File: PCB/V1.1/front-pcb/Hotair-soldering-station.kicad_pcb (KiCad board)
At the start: 2 copper layers, 99.4 x 61 mm, 24 parts, among them J1 Conn_01x03, J2 main-board-conn, J3 hot_on, SW1 HOTAIR_UP, SW2 HOTAIR_DOWN, SW3 SIRON_UP, SW4 SIRON_DOWN, SW5 FAN_UP, SW6 FAN_DOWN, SW7 MENU_UP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

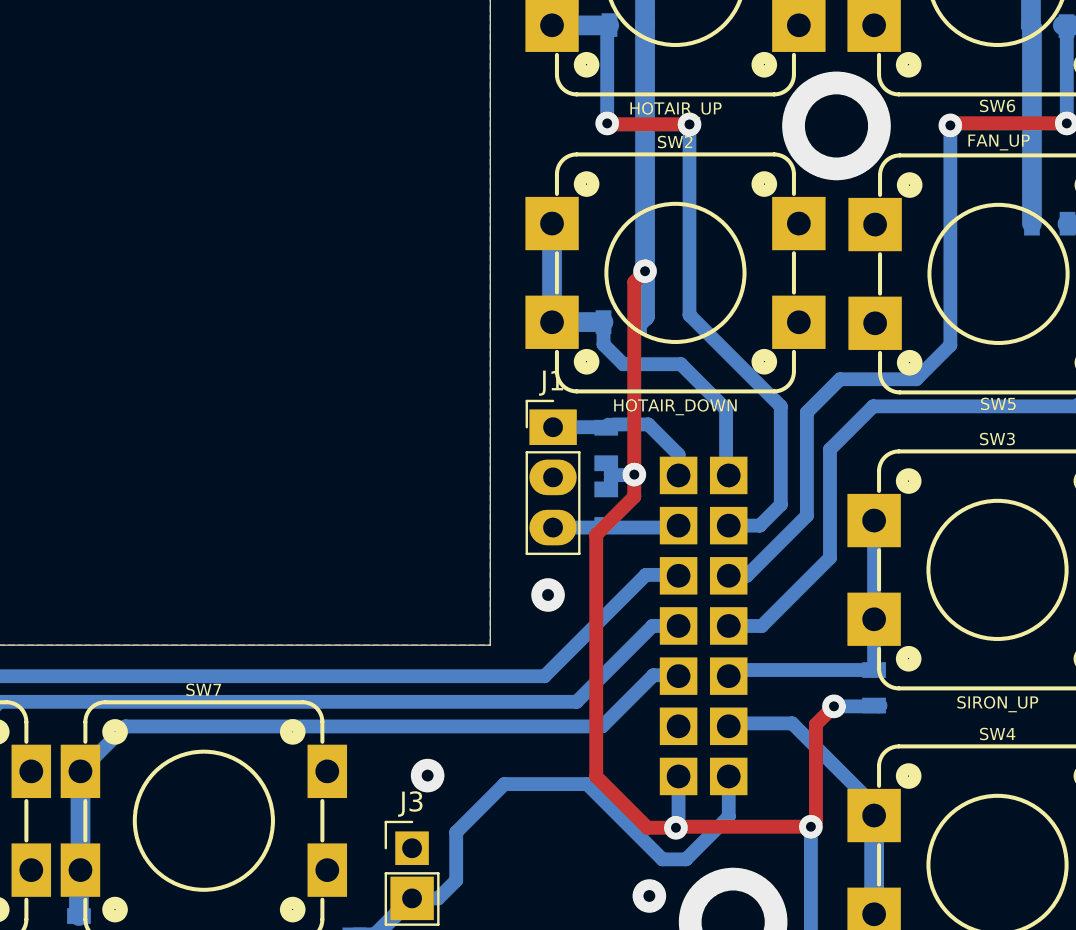
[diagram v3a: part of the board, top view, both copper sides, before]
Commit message: Larger IDC conenctor pads for front panel
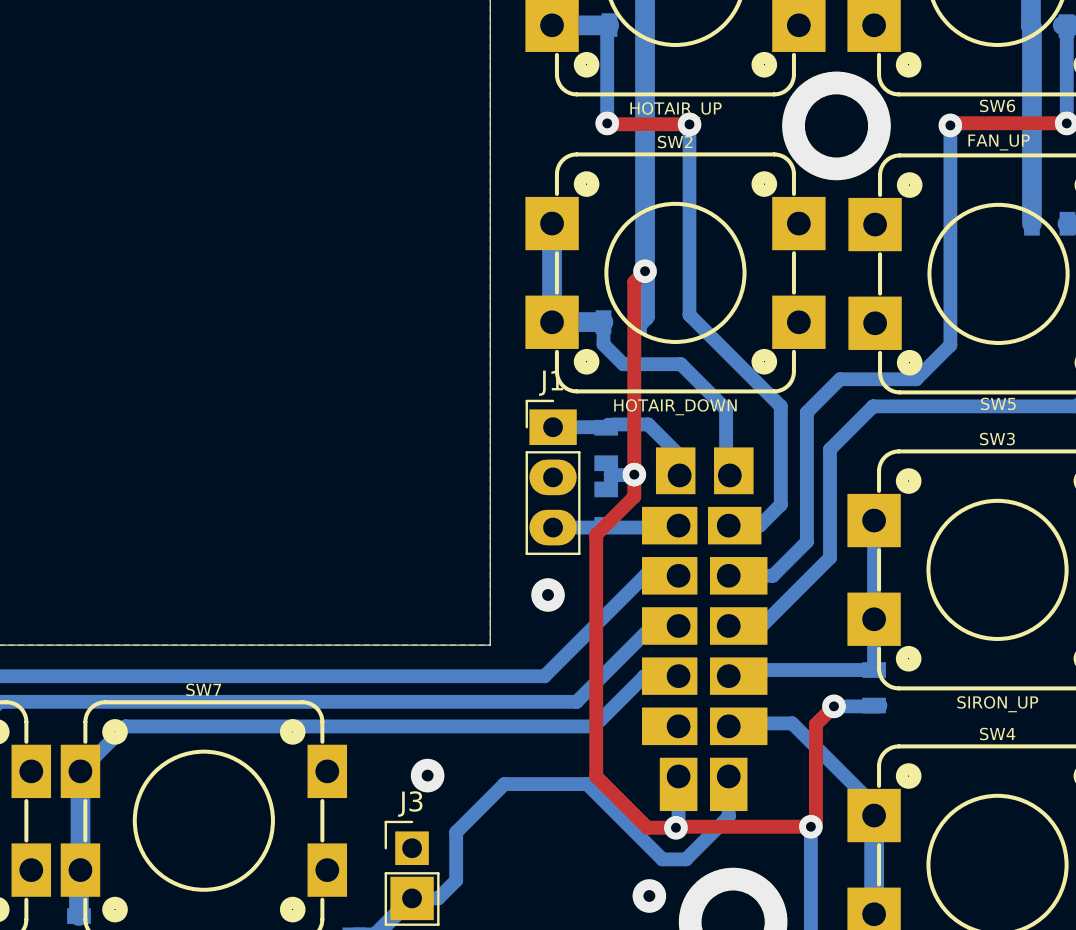
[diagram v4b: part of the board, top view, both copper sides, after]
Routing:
- net MENU_UP_SW: track 39.5 -> 40.8 mm
- net HOTAIR_FAN_DOWN_SW: track 49.1 -> 49.9 mm
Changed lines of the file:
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@@
     (property "Sheetname" "")
     (attr through_hole)
-    (fp_text reference "J2" (at 0 -0.5) (layer "B.SilkS")
+    (fp_text reference "J2" (at 0 -0.5 180) (layer "B.SilkS")
       (effects (font (size 1 1) (thickness 0.15)) (justify mirror))
     )
-    (fp_text value "main-board-conn" (at 0 0.5) (layer "B.Fab")
+    (fp_text value "main-board-conn" (at 0 0.5 180) (layer "B.Fab")
       (effects (font (size 1 1) (thickness 0.15)) (justify mirror))
     )
-    (fp_text user "REF**" (at 3.12 0.58) (layer "B.SilkS")
+    (fp_text user "REF**" (at 3.12 0.58 180) (layer "B.SilkS")
       (effects (font (size 1 1) (thickness 0.15)) (justify mirror))
     )
-    (fp_text user "${REFERENCE}" (at 3.12 -9.37 90) (layer "B.Fab")
+    (fp_text user "${REFERENCE}" (at 3.12 -9.37 -90) (layer "B.Fab")
       (effects (font (size 1 1) (thickness 0.15)) (justify mirror))
     )
@@
     (fp_line (start 5.66 -0.48) (end 5.66 -18.26) (layer "B.Fab") (width 0.1))
     (fp_line (start 0.58 -18.26) (end 0.58 -1.75) (layer "B.Fab") (width 0.1))
-    (pad "1" thru_hole rect locked (at 1.85 -1.75) (size 1.9 1.9) (drill 1.2) (layers *.Cu *.Mask)
+    (pad "1" thru_hole rect (at 1.85 -1.75) (size 1.9 2.7) (drill 1.2 (offset 0 0.4)) (layers *.Cu *.Mask)
       (net 7 "+3V3") (pinfunction "Pin_1") (pintype "passive"))
-    (pad "2" thru_hole rect locked (at 1.85 -4.29) (size 1.9 1.9) (drill 1.2) (layers *.Cu *.Mask)
+    (pad "2" thru_hole rect (at 1.85 -4.29) (size 2.8 1.9) (drill 1.2 (offset -0.45 0)) (layers *.Cu *.Mask)
       (net 6 "GND") (pinfunction "Pin_2") (pintype "passive"))
-    (pad "3" thru_hole rect locked (at 1.85 -6.83) (size 1.9 1.9) (drill 1.2) (layers *.Cu *.Mask)
+    (pad "3" thru_hole rect (at 1.85 -6.83) (size 2.8 1.9) (drill 1.2 (offset -0.45 0)) (layers *.Cu *.Mask)
       (net 8 "MENU_UP_SW") (pinfunction "Pin_3") (pintype "passive"))
-    (pad "4" thru_hole rect locked (at 1.85 -9.37) (size 1.9 1.9) (drill 1.2) (layers *.Cu *.Mask)
+    (pad "4" thru_hole rect (at 1.85 -9.37) (size 2.8 1.9) (drill 1.2 (offset -0.45 0)) (layers *.Cu *.Mask)
       (net 11 "MENU_OK_SW") (pinfunction "Pin_4") (pintype "passive"))
-    (pad "5" thru_hole rect locked (at 1.85 -11.91) (size 1.9 1.9) (drill 1.2) (layers *.Cu *.Mask)
+    (pad "5" thru_hole rect (at 1.85 -11.91) (size 2.8 1.9) (drill 1.2 (offset -0.45 0)) (layers *.Cu *.Mask)
       (net 12 "MENU_DOWN_SW") (pinfunction "Pin_5") (pintype "passive"))
-    (pad "6" thru_hole rect locked (at 1.85 -14.45) (size 1.9 1.9) (drill 1.2) (layers *.Cu *.Mask)
+    (pad "6" thru_hole rect (at 1.85 -14.45) (size 2.8 1.9) (drill 1.2 (offset -0.45 0)) (layers *.Cu *.Mask)
       (net 14 "T12_ON_SW") (pinfunction "Pin_6") (pintype "passive"))
-    (pad "7" thru_hole rect locked (at 1.85 -16.99) (size 1.9 1.9) (drill 1.2) (layers *.Cu *.Mask)
+    (pad "7" thru_hole rect (at 1.905 -16.99) (size 2 2.375) (drill 1.2 (offset -0.2 -0.2375)) (layers *.Cu *.Mask)
       (net 13 "WEP_ON_SW") (pinfunction "Pin_7") (pintype "passive"))
-    (pad "8" thru_hole rect locked (at 4.39 -16.99) (size 1.9 1.9) (drill 1.2) (layers *.Cu *.Mask)
+    (pad "8" thru_hole rect (at 4.445 -16.99) (size 2 2.375) (drill 1.2 (offset 0.2 -0.2375)) (layers *.Cu *.Mask)
       (net 2 "HOTAIR_DOWN_SW") (pinfunction "Pin_8") (pintype "passive"))
-    (pad "9" thru_hole rect locked (at 4.39 -14.45) (size 1.9 1.9) (drill 1.2) (layers *.Cu *.Mask)
+    (pad "9" thru_hole rect (at 4.39 -14.45) (size 2.7 1.9) (drill 1.2 (offset 0.3 0)) (layers *.Cu *.Mask)
       (net 1 "HOTAIR_UP_SW") (pinfunction "Pin_9") (pintype "passive"))
-    (pad "10" thru_hole rect locked (at 4.39 -11.91) (size 1.9 1.9) (drill 1.2) (layers *.Cu *.Mask)
+    (pad "10" thru_hole rect (at 4.39 -11.91) (size 2.91 1.9) (drill 1.2 (offset 0.505 0)) (layers *.Cu *.Mask)
       (net 10 "HOTAIR_FAN_DOWN_SW") (pinfunction "Pin_10") (pintype "passive"))
-    (pad "11" thru_hole rect locked (at 4.39 -9.37) (size 1.9 1.9) (drill 1.2) (layers *.Cu *.Mask)
+    (pad "11" thru_hole rect (at 4.39 -9.37) (size 2.91 1.9) (drill 1.2 (offset 0.505 0)) (layers *.Cu *.Mask)
       (net 9 "HOTAIR_FAN_UP_SW") (pinfunction "Pin_11") (pintype "passive"))
-    (pad "12" thru_hole rect locked (at 4.39 -6.83) (size 1.9 1.9) (drill 1.2) (layers *.Cu *.Mask)
+    (pad "12" thru_hole rect (at 4.39 -6.83) (size 2.91 1.9) (drill 1.2 (offset 0.505 0)) (layers *.Cu *.Mask)
       (net 3 "SOLDER_UP_SW") (pinfunction "Pin_12") (pintype "passive"))
-    (pad "13" thru_hole rect locked (at 4.39 -4.29) (size 1.9 1.9) (drill 1.2) (layers *.Cu *.Mask)
+    (pad "13" thru_hole rect (at 4.39 -4.29) (size 2.91 1.9) (drill 1.2 (offset 0.505 0)) (layers *.Cu *.Mask)
       (net 4 "SOLDER_DOWN_SW") (pinfunction "Pin_13") (pintype "passive"))
-    (pad "14" thru_hole rect locked (at 4.39 -1.75) (size 1.9 1.9) (drill 1.2) (layers *.Cu *.Mask)
+    (pad "14" thru_hole rect (at 4.39 -1.75) (size 1.9 2.7) (drill 1.2 (offset 0 0.4)) (layers *.Cu *.Mask)
       (net 5 "HOTAIR_ON_SW") (pinfunction "Pin_14") (pintype "passive"))
   )
@@
   (segment (start 160.13684 44.704) (end 160.13684 34.7472) (width 1) (layer "B.Cu") (net 7))
   (segment (start 111.9632 72.43064) (end 114.23904 70.1548) (width 0.7) (layer "B.Cu") (net 8))
-  (segment (start 114.23904 70.1548) (end 138.3792 70.1548) (width 0.7) (layer "B.Cu") (net 8))
   (segment (start 140.97 67.564) (end 142.113 67.564) (width 0.7) (layer "B.Cu") (net 8))
   (segment (start 111.887 79.756) (end 111.887 77.50556) (width 1) (layer "B.Cu") (net 8))
-  (segment (start 138.3792 70.1548) (end 140.97 67.564) (width 0.7) (layer "B.Cu") (net 8))
   (segment (start 111.9632 77.42936) (end 111.9632 72.43064) (width 1) (layer "B.Cu") (net 8))
   (segment (start 111.887 77.50556) (end 111.9632 77.42936) (width 1) (layer "B.Cu") (net 8))
+  (segment (start 114.23904 70.1548) (end 137.9728 70.1548) (width 0.7) (layer "B.Cu") (net 8))
+  (segment (start 140.5191 67.6085) (end 137.9728 70.1548) (width 0.7) (layer "B.Cu") (net 8))
+  (segment (start 142.2455 67.6085) (end 140.5191 67.6085) (width 0.7) (layer "B.Cu") (net 8))
   (segment (start 144.7855 65.0685) (end 146.4627 65.0685) (width 0.7) (layer "B.Cu") (net 9))
   (segment (start 162.4076 53.9496) (end 165.1 51.2572) (width 0.7) (layer "B.Cu") (net 9))
@@
   (via (at 161.8996 39.624) (size 1.2) (drill 0.5) (layers "F.Cu" "B.Cu") (net 10))
   (via (at 156.0068 39.7256) (size 1.2) (drill 0.5) (layers "F.Cu" "B.Cu") (net 10))
+  (segment (start 150.4188 52.578) (end 148.7424 54.2544) (width 0.7) (layer "B.Cu") (net 10))
+  (segment (start 148.7424 60.8076) (end 147.0215 62.5285) (width 0.7) (layer "B.Cu") (net 10))
   (segment (start 164.63772 34.66084) (end 164.6428 34.65576) (width 1) (layer "B.Cu") (net 10))
-  (segment (start 145.7007 62.5285) (end 148.7424 59.4868) (width 0.7) (layer "B.Cu") (net 10))
-  (segment (start 156.0068 50.8508) (end 156.0068 39.7256) (width 0.7) (layer "B.Cu") (net 10))
+  (segment (start 154.2796 52.578) (end 150.4188 52.578) (width 0.7) (layer "B.Cu") (net 10))
+  (segment (start 147.0215 62.5285) (end 144.7855 62.5285) (width 0.7) (layer "B.Cu") (net 10))
+  (segment (start 148.7424 54.2544) (end 148.7424 60.8076) (width 0.7) (layer "B.Cu") (net 10))
   (segment (start 164.6428 34.65576) (end 164.6428 29.65704) (width 1) (layer "B.Cu") (net 10))
-  (segment (start 150.4188 52.578) (end 154.2796 52.578) (width 0.7) (layer "B.Cu") (net 10))
-  (segment (start 148.7424 59.4868) (end 148.7424 54.2544) (width 0.7) (layer "B.Cu") (net 10))
+  (segment (start 156.0068 50.8508) (end 154.2796 52.578) (width 0.7) (layer "B.Cu") (net 10))
   (segment (start 161.8996 39.624) (end 161.8996 34.6456) (width 0.7) (layer "B.Cu") (net 10))
-  (segment (start 154.2796 52.578) (end 156.0068 50.8508) (width 0.7) (layer "B.Cu") (net 10))
-  (segment (start 148.7424 54.2544) (end 150.4188 52.578) (width 0.7) (layer "B.Cu") (net 10))
   (segment (start 161.6964 34.66084) (end 164.63772 34.66084) (width 1) (layer "B.Cu") (net 10))
-  (segment (start 144.7855 62.5285) (end 145.7007 62.5285) (width 0.7) (layer "B.Cu") (net 10))
+  (segment (start 156.0068 39.7256) (end 156.0068 50.8508) (width 0.7) (layer "B.Cu") (net 10))
   (segment (start 96.901 77.45476) (end 96.9772 77.37856) (width 1) (layer "B.Cu") (net 11))
   (segment (start 96.9772 72.43064) (end 104.35336 72.43064) (width 0.7) (layer "B.Cu") (net 11))

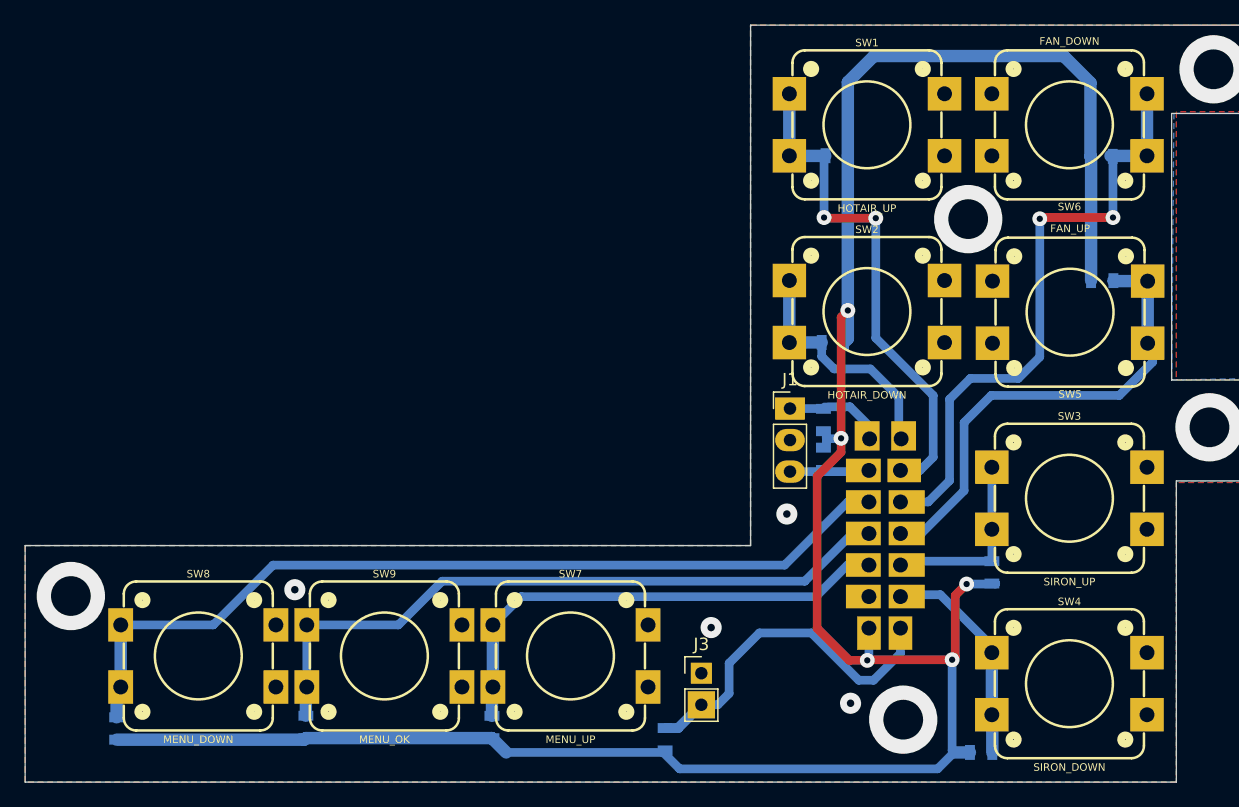
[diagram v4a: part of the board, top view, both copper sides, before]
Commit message: T12 and WEP tests done
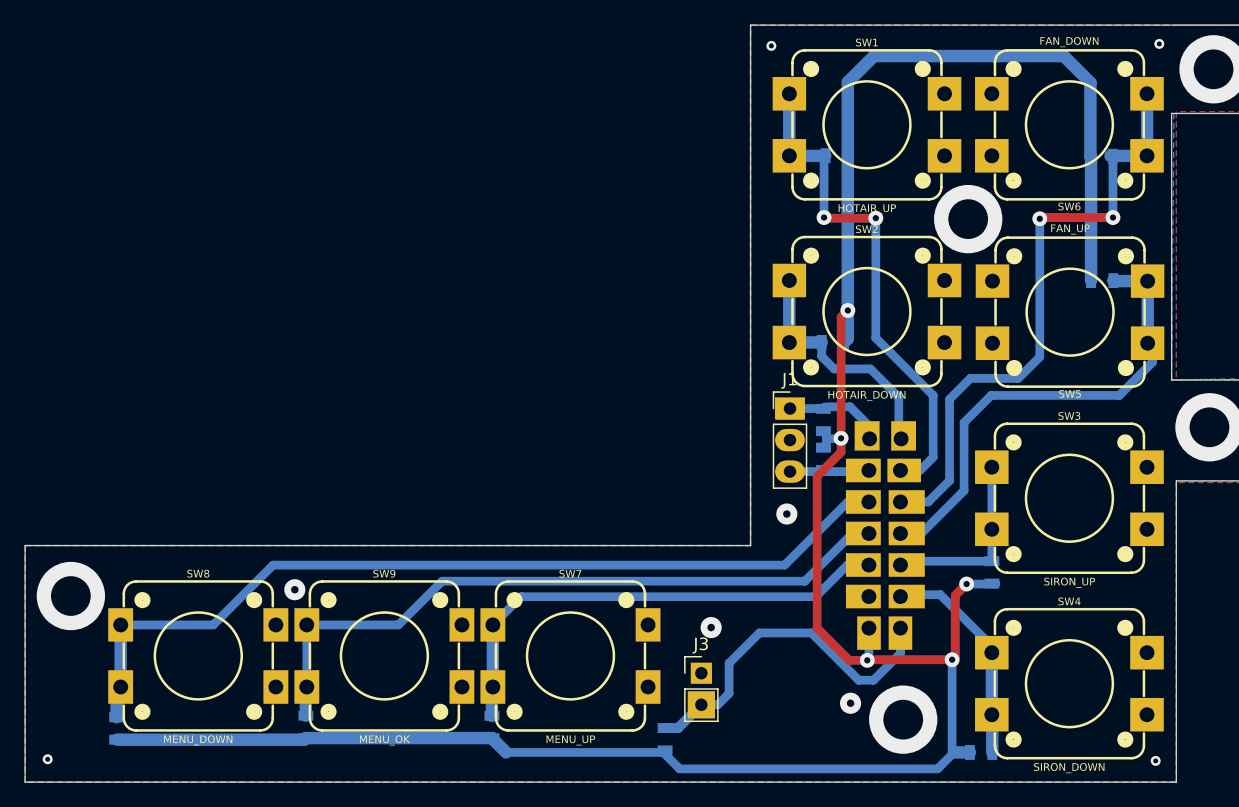
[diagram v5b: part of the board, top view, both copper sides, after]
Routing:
- net GND: vias 9 -> 13
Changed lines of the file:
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@@
   (gr_circle (center 103.211883 74.885863) (end 107.711883 74.885863) (layer "Dwgs.User") (width 0.2) (fill none))
   (gr_line (start 53.466381 32.347107) (end 124.766381 32.347107) (layer "Dwgs.User") (width 0.2))
+  (gr_line (start 105.21 98.01) (end 106.13 286.63) (layer "Cmts.User") (width 0.1))
   (gr_poly
     (pts
@@
   (via (at 96.012 69.596) (size 1.7) (drill 0.6) (layers "F.Cu" "B.Cu") (free) (net 6))
   (via (at 129.54 72.644) (size 1.7) (drill 0.6) (layers "F.Cu" "B.Cu") (free) (net 6))
+  (via (at 165.63 25.64) (size 0.8) (drill 0.4) (layers "F.Cu" "B.Cu") (free) (net 6))
   (via (at 135.636 63.5) (size 1.7) (drill 0.6) (layers "F.Cu" "B.Cu") (free) (net 6))
+  (via (at 76.11 83.25) (size 0.8) (drill 0.4) (layers "F.Cu" "B.Cu") (free) (net 6))
   (via (at 77.978 70.104) (size 5.5) (drill 3.2) (layers "F.Cu" "B.Cu") (free) (net 6))
+  (via (at 134.39 25.8) (size 0.8) (drill 0.4) (layers "F.Cu" "B.Cu") (free) (net 6))
   (via (at 145.0086 80.0608) (size 5.5) (drill 3.2) (layers "F.Cu" "B.Cu") (free) (net 6))
   (via (at 170 27.686) (size 5.5) (drill 3.2) (layers "F.Cu" "B.Cu") (free) (net 6))
   (via (at 169.672 56.515) (size 5.5) (drill 3.2) (layers "F.Cu" "B.Cu") (free) (net 6))
   (via (at 140.7668 78.74) (size 1.7) (drill 0.6) (layers "F.Cu" "B.Cu") (free) (net 6))
+  (via (at 165.34 83.38) (size 0.8) (drill 0.4) (layers "F.Cu" "B.Cu") (free) (net 6))
   (via (at 150.241 39.751) (size 5.5) (drill 3.2) (layers "F.Cu" "B.Cu") (free) (net 6))
   (segment (start 148.9456 75.2348) (end 149.1996 74.9808) (width 0.7) (layer "F.Cu") (net 7))
